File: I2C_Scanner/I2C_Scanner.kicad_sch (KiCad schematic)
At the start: 57 parts, among them J1 USB_B_Micro, J2 Conn_01x02_Pin, J3 Conn_01x04_Pin, J4 Conn_01x04_Pin, J5 Conn_01x20_Pin, SW1 SW_Push, SW2 SW_Push, U1 RP2040, U2 NCP1117-3.3_SOT223, U3 W25Q128JVS, U4 NCP1117-1.8_SOT223, U5 TXS0108EPW, U6 TXS0108EPW, U7 TXS0108EPW, Y1 ABM8-272-T3

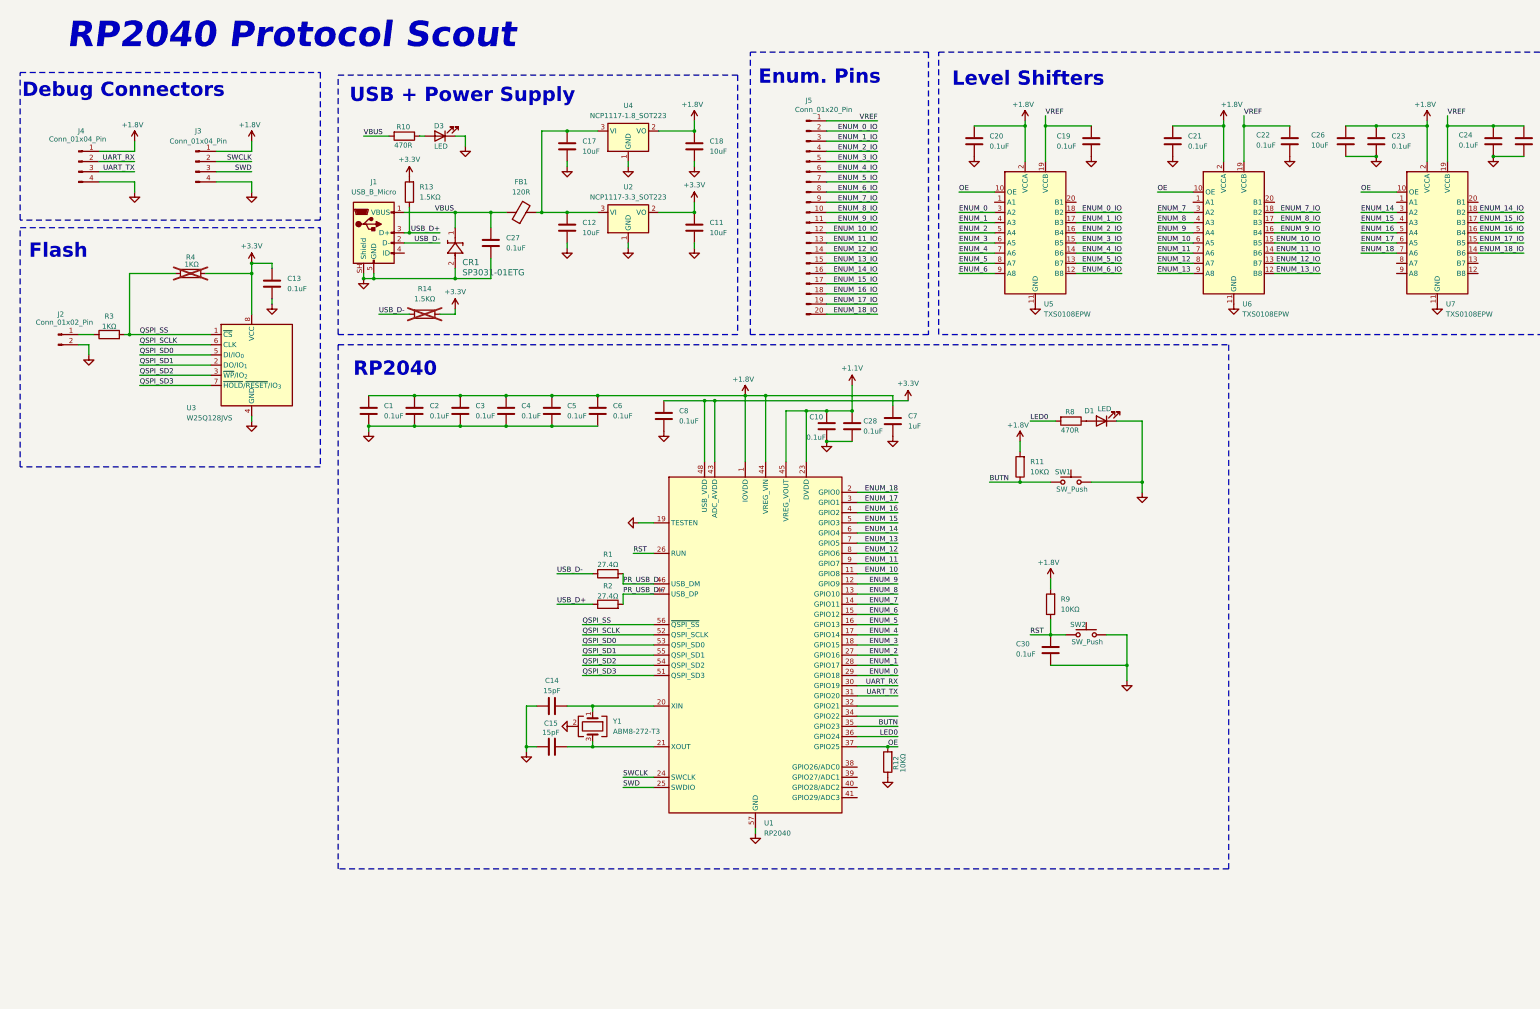
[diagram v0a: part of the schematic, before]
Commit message: Added USB C
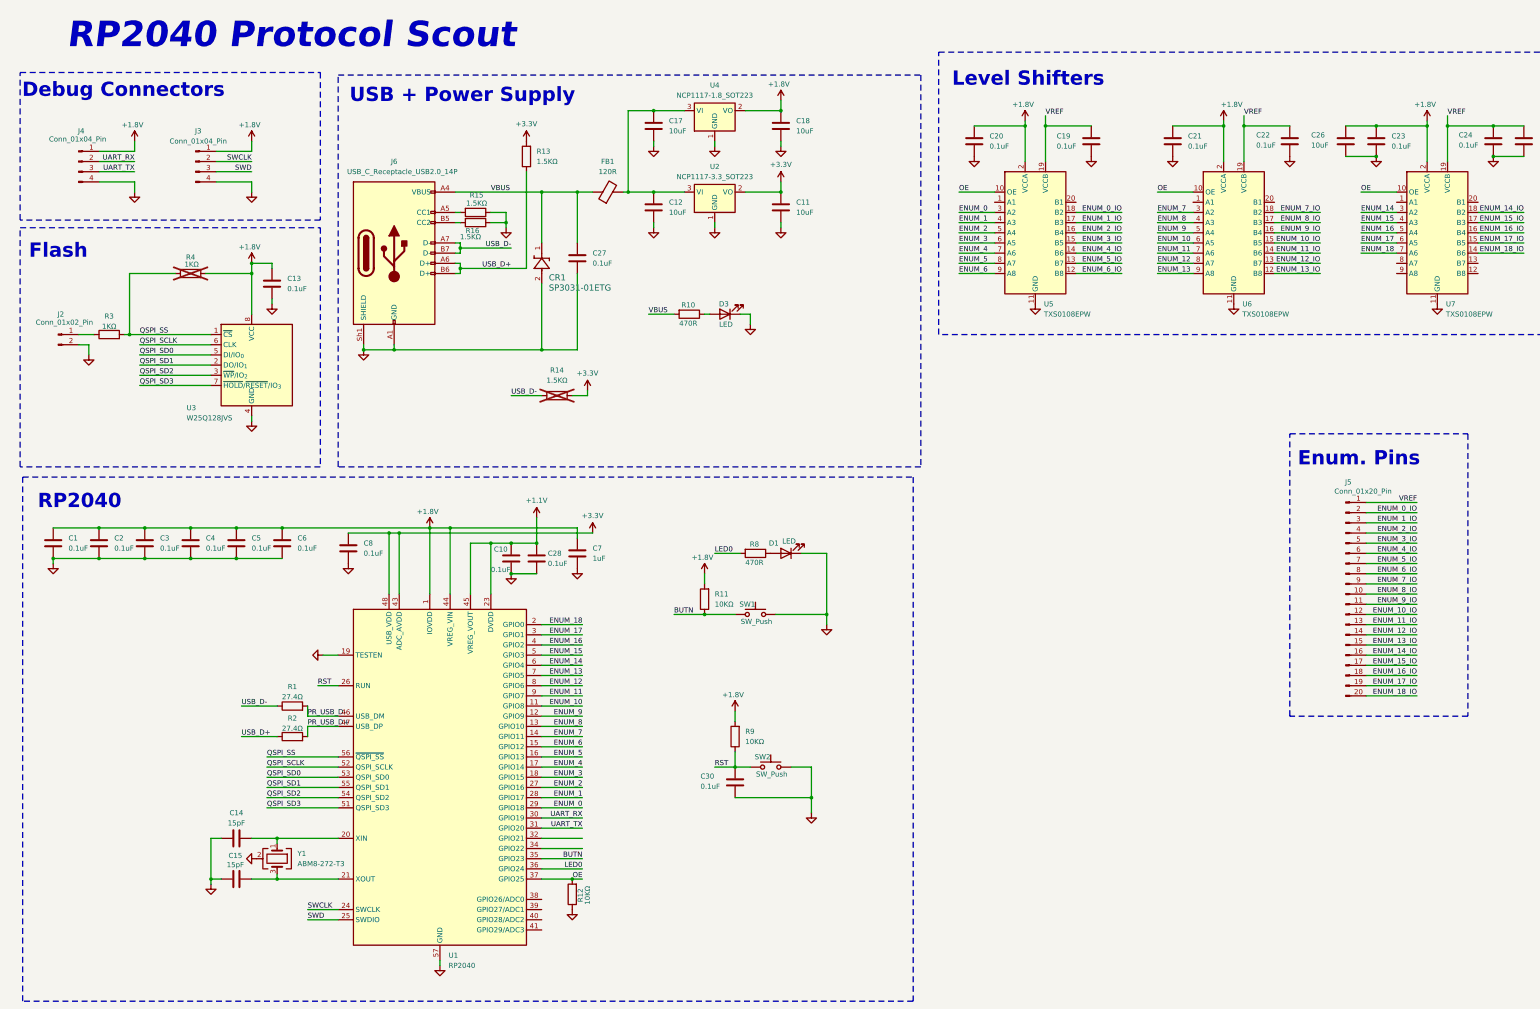
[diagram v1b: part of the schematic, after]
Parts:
- removed J1: USB_B_Micro, Connector_USB:USB_Micro-B_Wuerth_629105150521, symbol Connector:USB_B_Micro
- added J6: USB_C_Receptacle_USB2.0_14P, USB_C_Footprint:TYPE-C-31-M-14, symbol Connector:USB_C_Receptacle_USB2.0_14P
- added R15, R16: 1.5KΩ, Resistor_SMD:R_0402_1005Metric, symbol Device:R
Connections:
- net +1.8V: now also C13.1, R4.2, U3.8 (VCC)
- net +3.3V: no longer C13.1, R4.2, U3.8 (VCC)
- net GND: now also J6.A1 (GND), J6.A12 (GND), J6.B1 (GND), J6.B12 (GND), J6.Sh1 (SHIELD), R15.1, R16.1
- net USB_D+: now also J6.A6 (D+), J6.B6 (D+)
- net USB_D-: now also J6.A7 (D-), J6.B7 (D-)
- net VBUS: now also J6.A4 (VBUS), J6.A9 (VBUS), J6.B4 (VBUS), J6.B9 (VBUS)
- new net: J6.A5 (CC1), R15.2
- new net: J6.B5 (CC2), R16.2
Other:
- moved on the sheet: C1, C10, C11, C12, C14, C15, C17, C18, C2, C27, C28, C3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

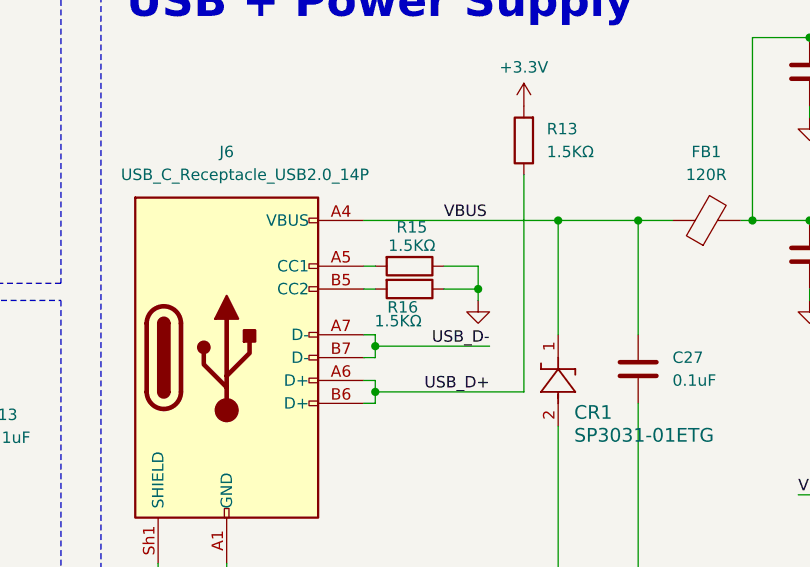
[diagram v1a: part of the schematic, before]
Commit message: Changed CC Resitor Values
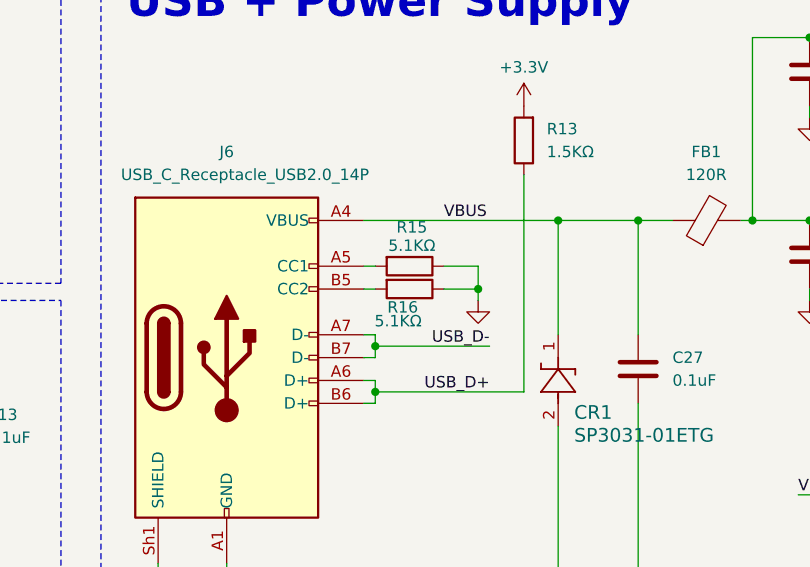
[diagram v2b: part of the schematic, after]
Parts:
- R15, R16: value 1.5KΩ -> 5.1KΩ
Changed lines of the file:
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@@
 			)
 		)
-		(property "Value" "1.5KΩ"
+		(property "Value" "5.1KΩ"
 			(at 130.81 70.866 90)
 			(show_name no)
@@
 			)
 		)
-		(property "Value" "1.5KΩ"
+		(property "Value" "5.1KΩ"
 			(at 132.334 62.484 90)
 			(show_name no)
